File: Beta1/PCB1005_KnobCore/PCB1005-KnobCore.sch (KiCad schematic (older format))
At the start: 34 parts, among them J1 Axoloti_40Pin, U10 OLED_128x32_I2C, U1000 MCP3008T-I/SL, U2 MCP3008T-I/SL, U20 OLED_128x32_I2C, U30 OLED_128x32_I2C, U40 OLED_128x32_I2C, U5 I2C_1x4MUX_TCA9546A

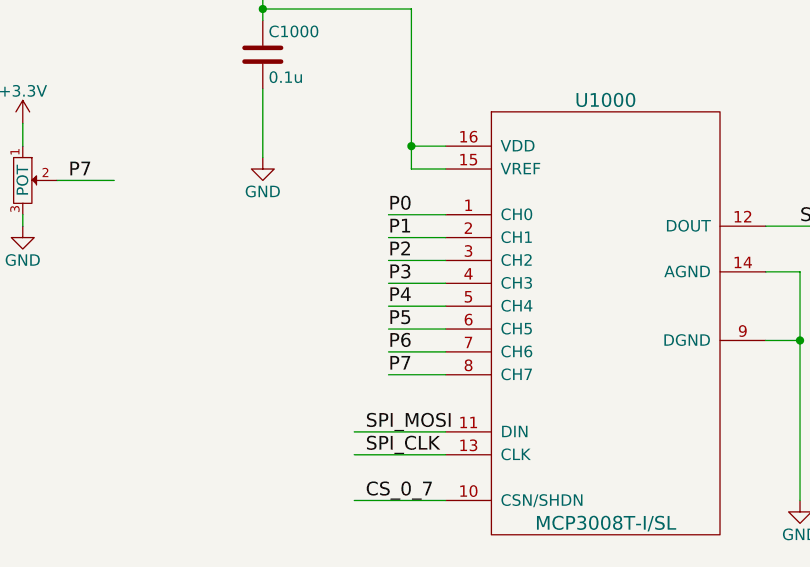
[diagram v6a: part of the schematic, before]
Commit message: Initial routing complete. Waiting on pinouts to finish
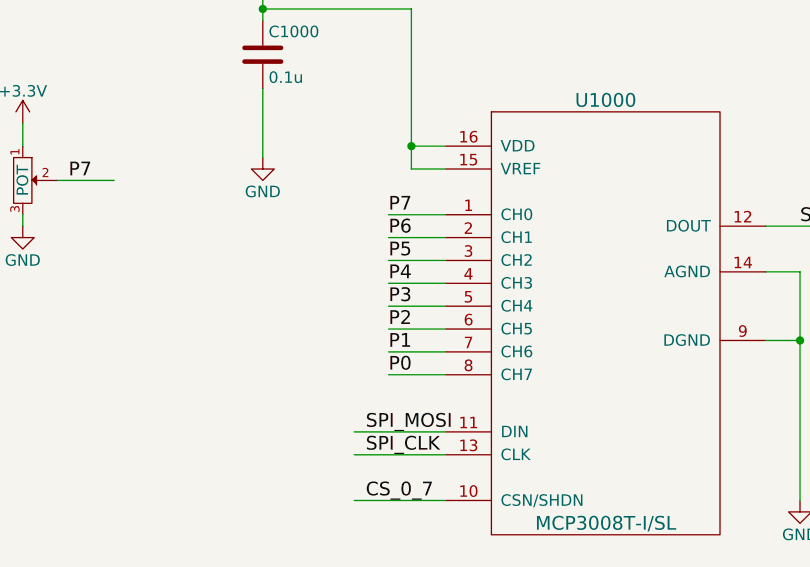
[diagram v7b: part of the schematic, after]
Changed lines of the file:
@@
 $EndComp
 Text Label 9550 1700 0    60   ~ 0
-P0
+P7
 $Comp
 L GND #PWR019
@@
 $EndComp
 Text Label 9550 1800 0    60   ~ 0
+P6
+Text Label 9550 1900 0    60   ~ 0
+P5
+Text Label 9550 2000 0    60   ~ 0
+P4
+Text Label 9550 2100 0    60   ~ 0
+P3
+Text Label 9550 2200 0    60   ~ 0
+P2
+Text Label 9550 2300 0    60   ~ 0
 P1
-Text Label 9550 1900 0    60   ~ 0
-P2
-Text Label 9550 2000 0    60   ~ 0
-P3
-Text Label 9550 2100 0    60   ~ 0
-P4
-Text Label 9550 2200 0    60   ~ 0
-P5
-Text Label 9550 2300 0    60   ~ 0
-P6
 Text Label 9550 2400 0    60   ~ 0
-P7
+P0
 $Comp
 L MCP3008T-I/SL U2

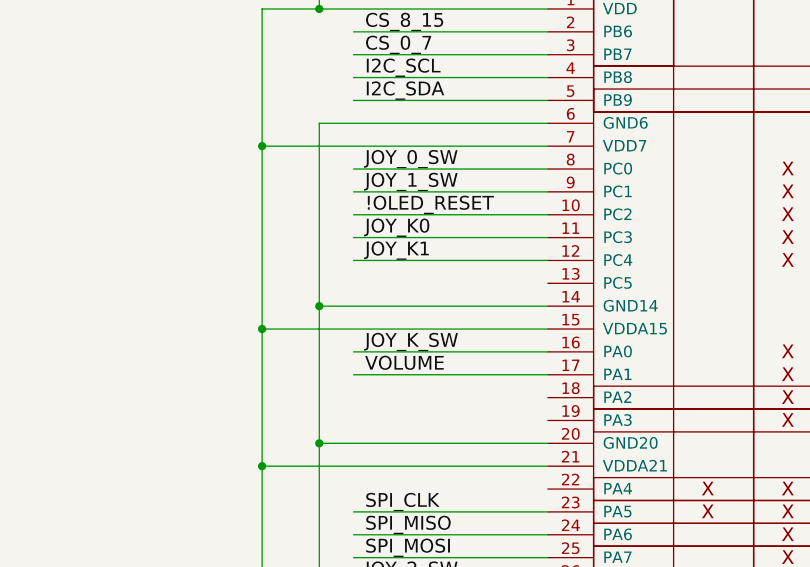
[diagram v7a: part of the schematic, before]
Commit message: Moved Joystics to 30mm from Knobs
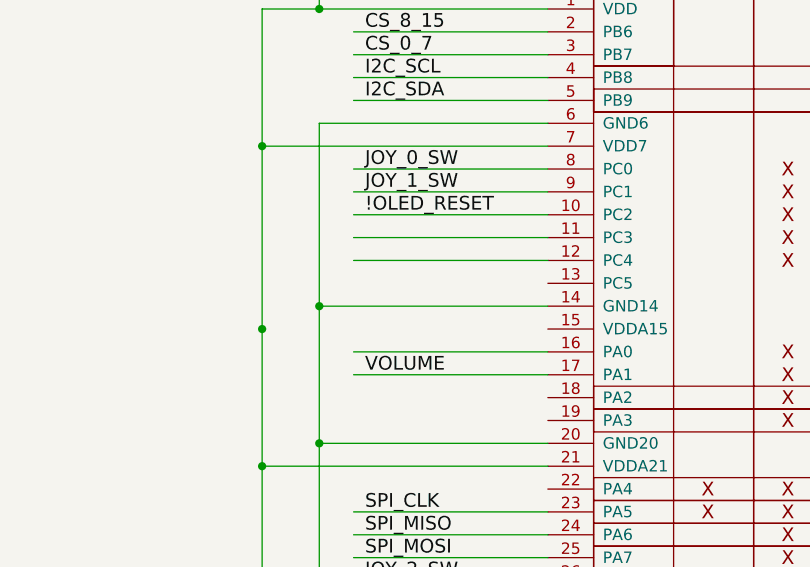
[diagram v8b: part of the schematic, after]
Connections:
- net labels removed: JOY_K0, JOY_K1, JOY_K_SW
- wire segments 201 -> 200
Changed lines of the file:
@@
 	14650 2700 15900 2700
-Wire Wire Line
-	14650 3500 15900 3500
 Wire Wire Line
 	14650 4100 15900 4100
@@
 	26450 4900 27550 4900
 Connection ~ 26450 3950
-Text Label 15100 3100 0    60   ~ 0
-JOY_K0
-Text Label 15100 3200 0    60   ~ 0
-JOY_K1
-Text Label 15100 3600 0    60   ~ 0
-JOY_K_SW
 Wire Wire Line
 	15900 3100 15050 3100
